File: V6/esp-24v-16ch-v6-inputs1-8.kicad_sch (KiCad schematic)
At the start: 10 parts, among them U9 OR-3H7-4

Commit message: V6 is up
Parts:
- renumbered C30 to C38, C31 to C39, D9 to D10, D10 to D11, D11 to D12, R40 to R41, R41 to R42, R42 to R43, U9 to U10
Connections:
- net GND: now also U10.9; no longer C38.2, C39.2, D10.2 (A2), D11.1 (K), U10.15, U10.2
- net INOPTO: now also U10.7; no longer U10.1
- net MUXIN: now also U10.10; no longer U10.16
- new net GNDIO: C38.2, C39.2, D10.2 (A2), D11.1 (K), U10.8

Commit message: Revising power rails
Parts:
- renumbered C38 to C39, C39 to C40

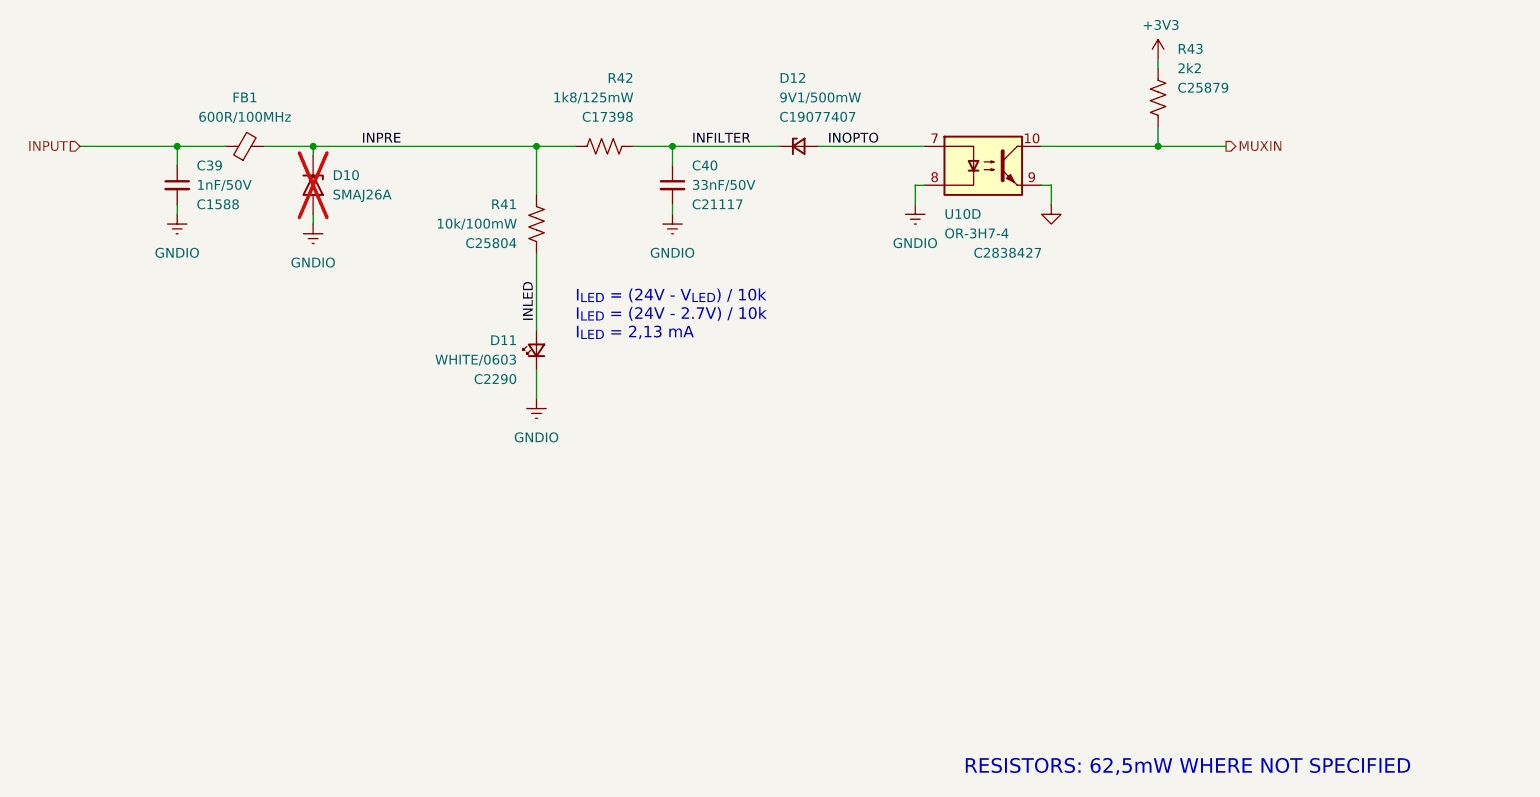
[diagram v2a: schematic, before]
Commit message: Added voltage monitors for both ESP32 and LAN8710A
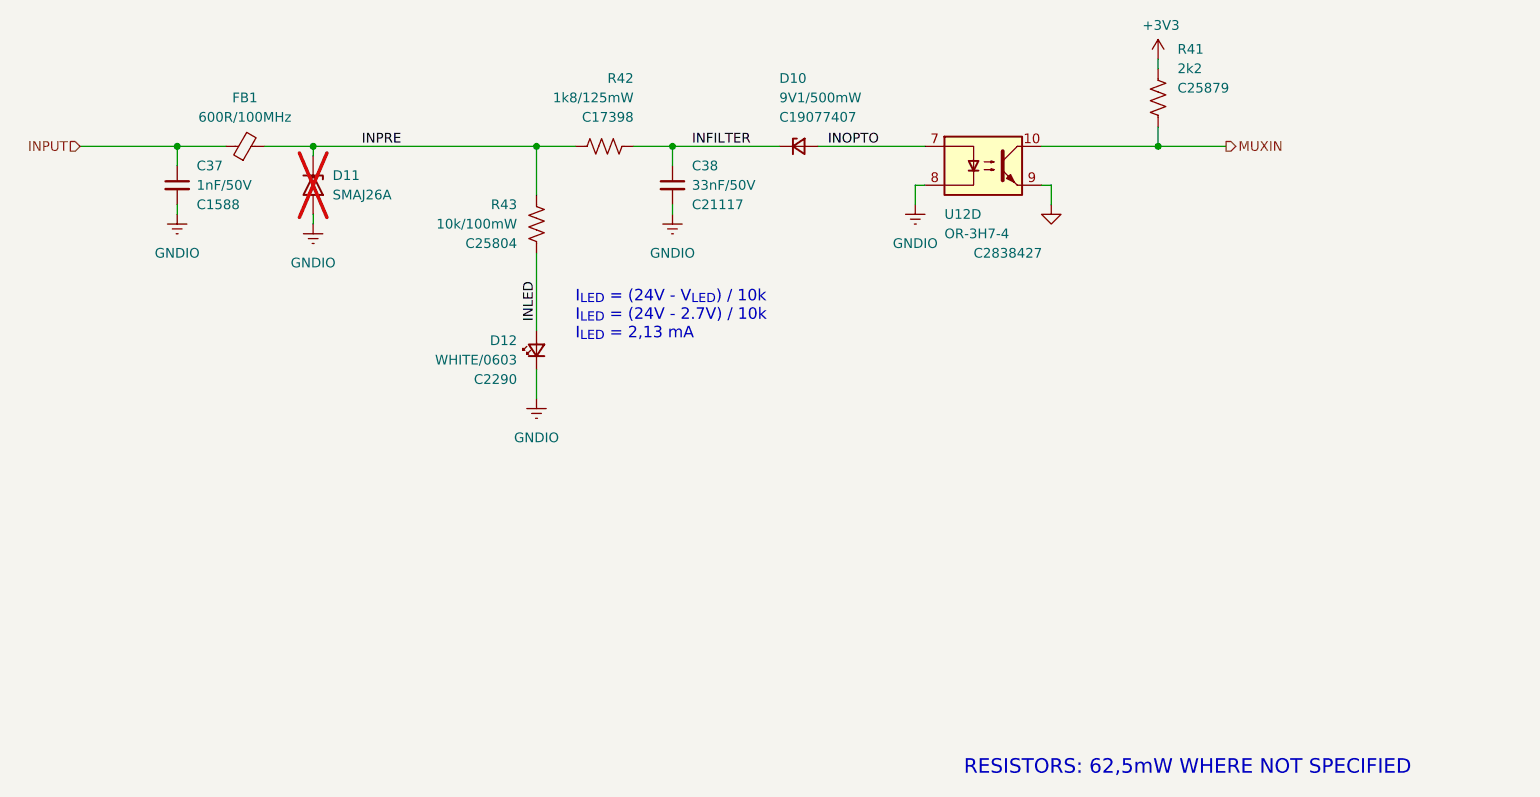
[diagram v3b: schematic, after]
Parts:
- renumbered C39 to C37, C40 to C38, D12 to D10, D10 to D11, D11 to D12, R43 to R41, R41 to R43, U10 to U12
